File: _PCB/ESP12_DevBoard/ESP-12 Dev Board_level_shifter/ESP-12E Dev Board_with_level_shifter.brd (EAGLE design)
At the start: 52 x 60 mm, 50 parts, among them J1 ZX62-B-5PA(33), J10 BTN1, J11 BTN2, J2 I2C, J3 LCD, J4 I2C, J5 LCD_BACKLIGHT, J6 TEMP/HUM, J7 RADON, J8 DUST, J9 ADC, Q1 UMH3N, U1 5V_REG, U2 3V3_REG, U3 CH340C, U4 TXS0104

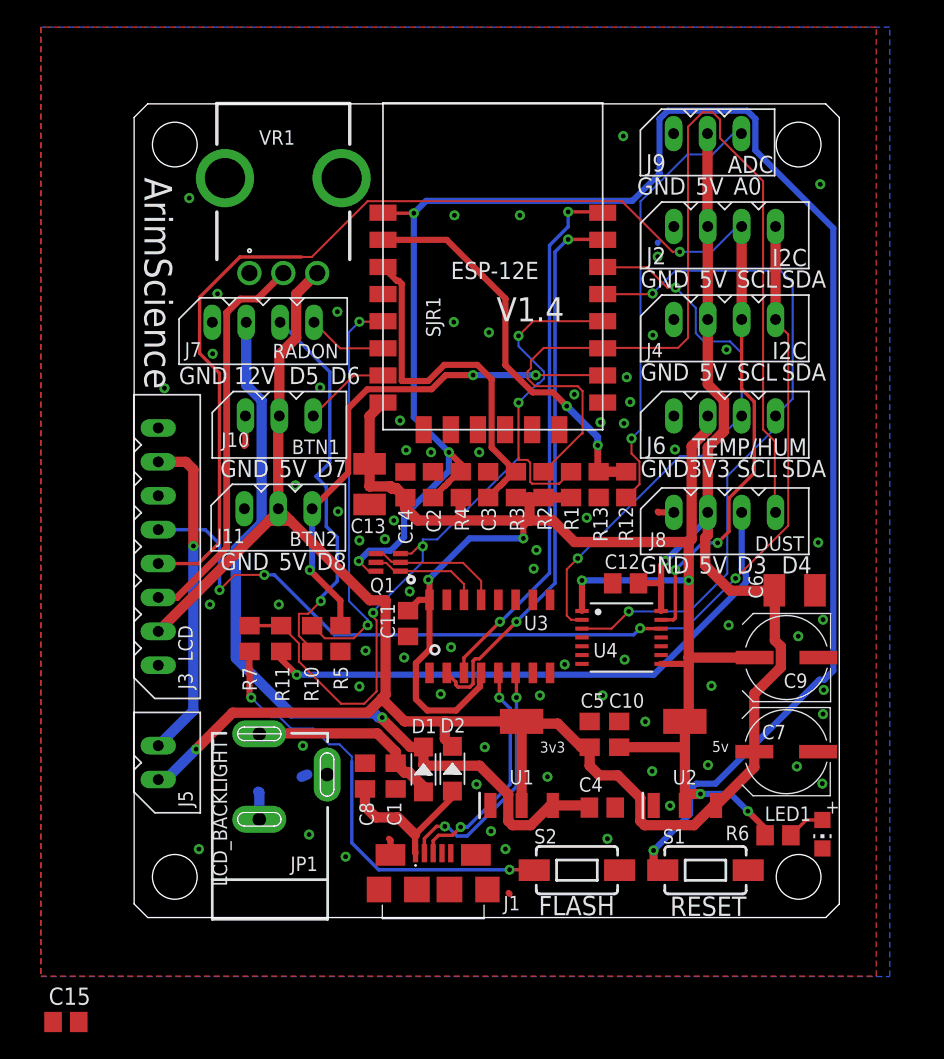
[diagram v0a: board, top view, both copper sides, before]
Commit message: ESP12 dev board PCB update
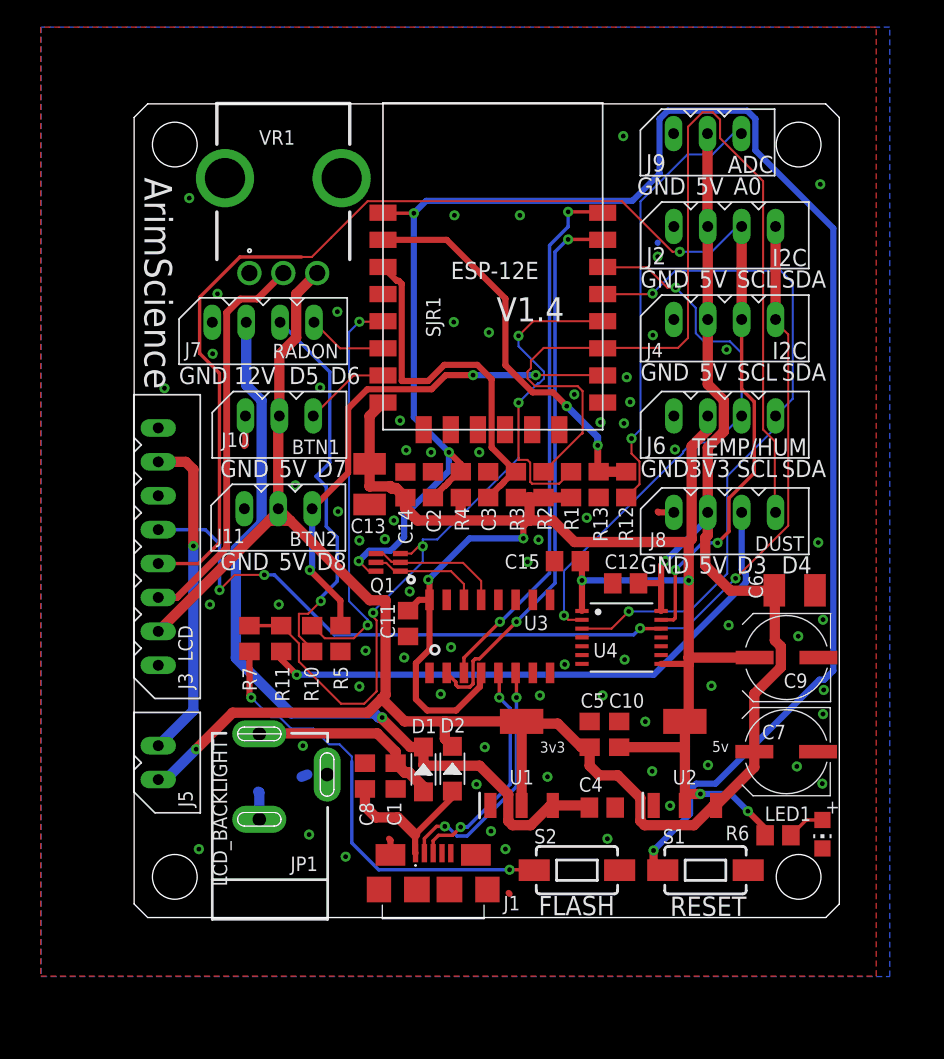
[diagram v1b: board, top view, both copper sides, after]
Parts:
- moved C15 50.2 mm to (32.0, 24.3)
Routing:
- net 3.3V: track 127.2 -> 128.7 mm

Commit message: ESP-12E Dev Board level shifter edit
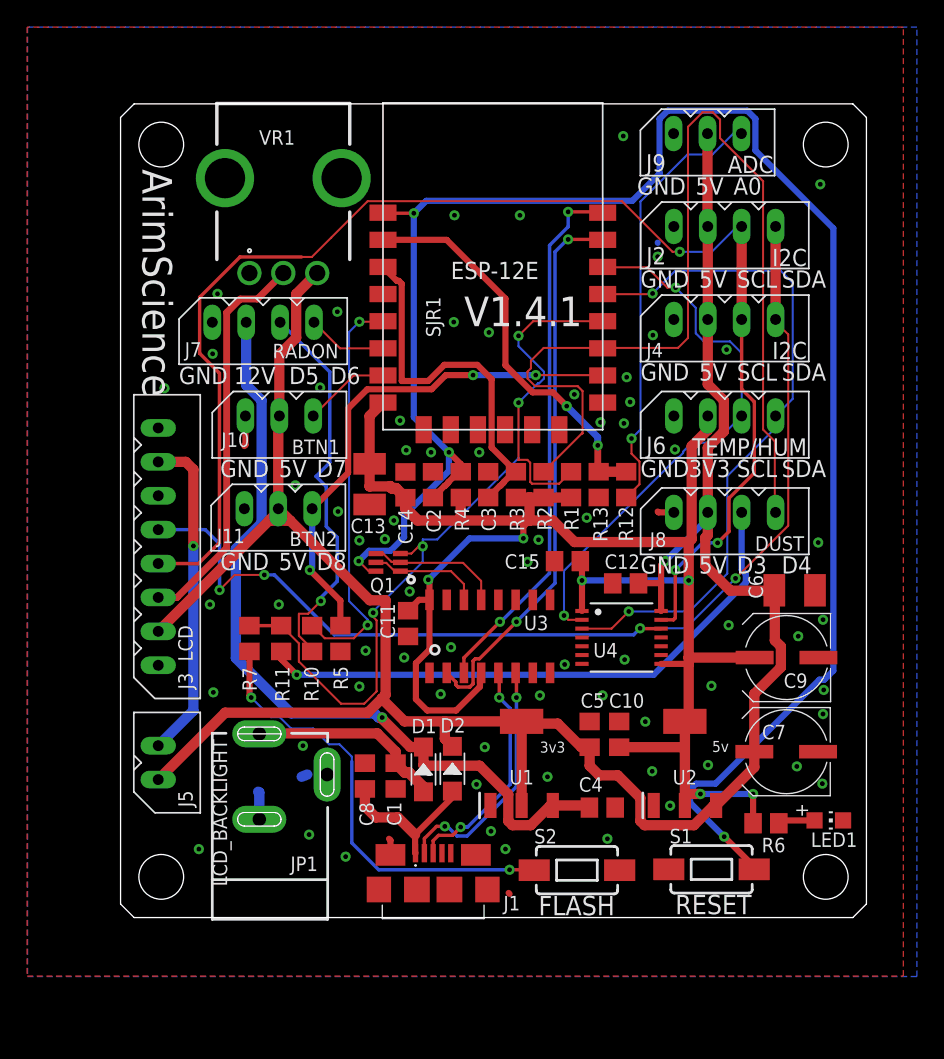
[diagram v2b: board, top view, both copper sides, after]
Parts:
- moved R6 1.26 mm to (46.6, 4.95)
- moved LED1 1.12 mm to (51.2, 5.16), turned to 270 degrees
- moved S1 0.45 mm to (42.6, 1.56), turned to 180 degrees
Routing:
- net 5V: vias 2 -> 1
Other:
- board size 52 x 60 mm -> 55 x 60 mm
- board text added: "V1.4.1"
- board text removed: "V1.4"
